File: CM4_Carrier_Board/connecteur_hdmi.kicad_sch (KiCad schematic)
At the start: 3 parts, among them J5 HDMI_A

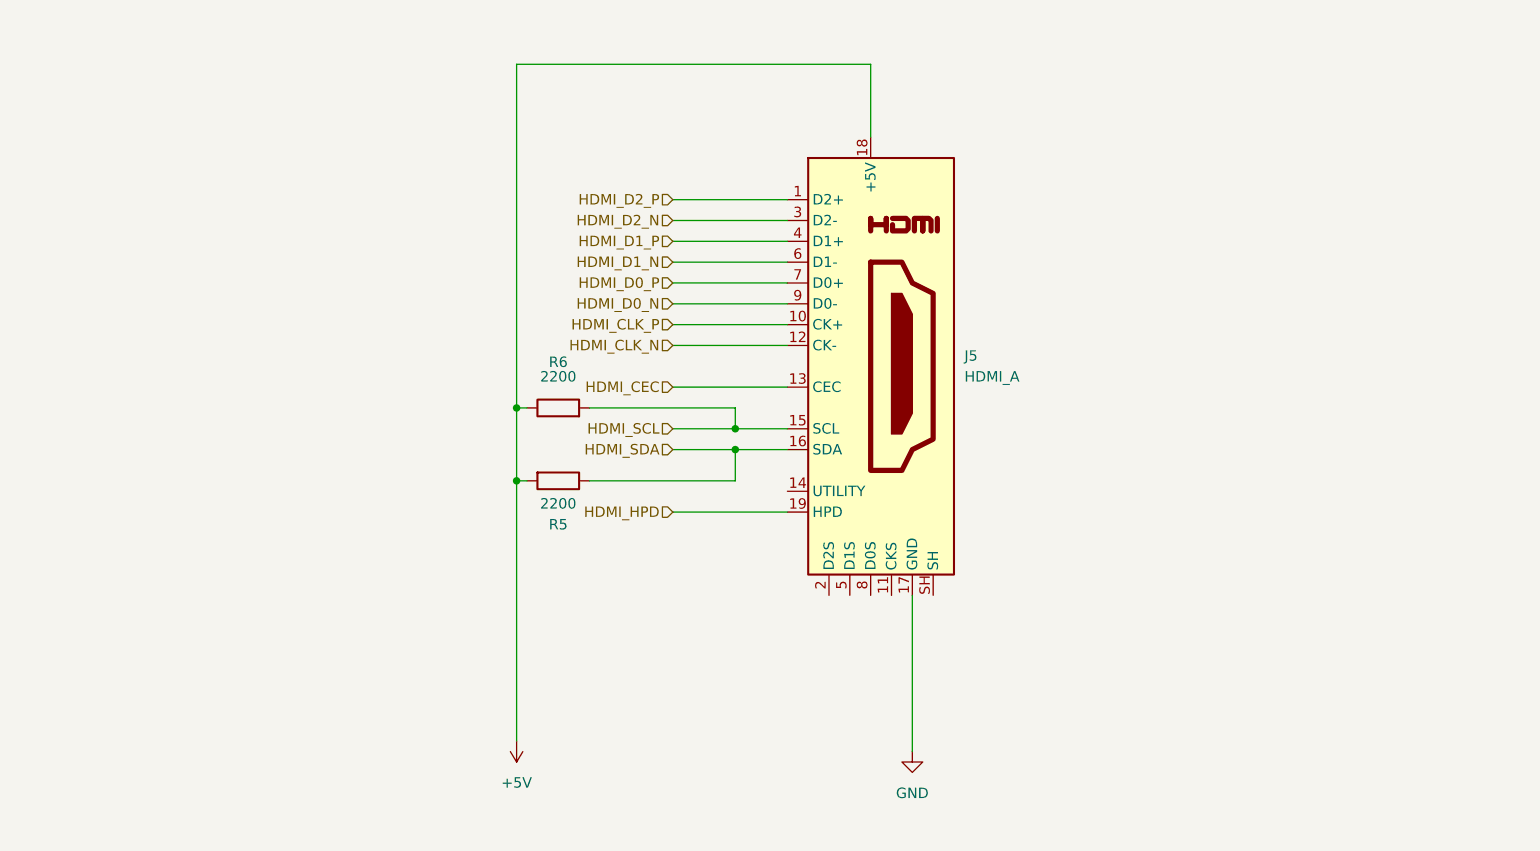
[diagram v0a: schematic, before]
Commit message: Implementation du bloc HDMI
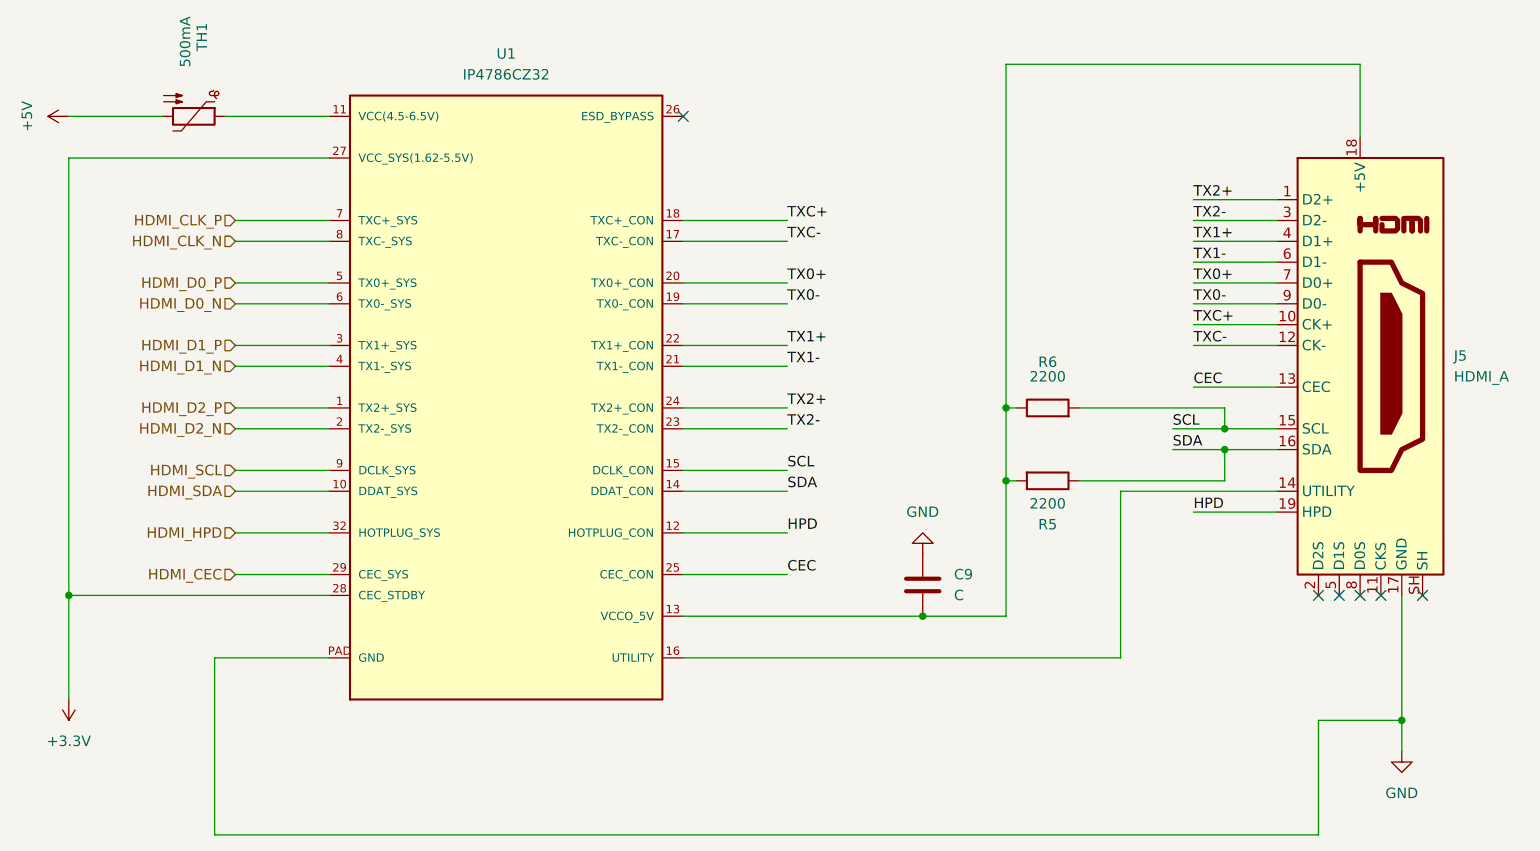
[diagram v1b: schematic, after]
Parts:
- added C9: C, symbol Device:C
- added TH1: 500mA, symbol Device:Thermistor_PTC
- added U1: IP4786CZ32, IP4786CZ32:HVQFN32, symbol IP4786CZ32:IP4786CZ32
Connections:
- net +5V: now also TH1.2; no longer J5.18 (+5V), R5.2, R6.1
- net GND: now also C9.1, U1.PAD (GND)
- net HDMI_CEC: now also U1.29 (CEC_SYS); no longer J5.13 (CEC)
- net HDMI_CLK_N: now also U1.8 (TXC-_SYS); no longer J5.12 (CK-)
- net HDMI_CLK_P: now also U1.7 (TXC+_SYS); no longer J5.10 (CK+)
- net HDMI_D0_N: now also U1.6 (TX0-_SYS); no longer J5.9 (D0-)
- net HDMI_D0_P: now also U1.5 (TX0+_SYS); no longer J5.7 (D0+)
- net HDMI_D1_N: now also U1.4 (TX1-_SYS); no longer J5.6 (D1-)
- net HDMI_D1_P: now also U1.3 (TX1+_SYS); no longer J5.4 (D1+)
- net HDMI_D2_N: now also U1.2 (TX2-_SYS); no longer J5.3 (D2-)
- net HDMI_D2_P: now also U1.1 (TX2+_SYS); no longer J5.1 (D2+)
- net HDMI_HPD: now also U1.32 (HOTPLUG_SYS); no longer J5.19 (HPD)
- net HDMI_SCL: now also U1.9 (DCLK_SYS); no longer J5.15 (SCL), R6.2
- net HDMI_SDA: now also U1.10 (DDAT_SYS); no longer J5.16 (SDA), R5.1
- net at J5.14 (UTILITY): now also U1.16 (UTILITY)
- new net: TH1.1, U1.11 (VCC(4.5-6.5V))
- new net: C9.2, J5.18 (+5V), R5.2, R6.1, U1.13 (VCCO_5V)
- new net +3.3V: U1.27 (VCC_SYS(1.62-5.5V)), U1.28 (CEC_STDBY)
- new net CEC: J5.13 (CEC), U1.25 (CEC_CON)
- new net HPD: J5.19 (HPD), U1.12 (HOTPLUG_CON)
- new net SCL: J5.15 (SCL), R6.2, U1.15 (DCLK_CON)
- new net SDA: J5.16 (SDA), R5.1, U1.14 (DDAT_CON)
- new net TX0+: J5.7 (D0+), U1.20 (TX0+_CON)
- new net TX0-: J5.9 (D0-), U1.19 (TX0-_CON)
- new net TX1+: J5.4 (D1+), U1.22 (TX1+_CON)
- new net TX1-: J5.6 (D1-), U1.21 (TX1-_CON)
- new net TX2+: J5.1 (D2+), U1.24 (TX2+_CON)
- new net TX2-: J5.3 (D2-), U1.23 (TX2-_CON)
- new net TXC+: J5.10 (CK+), U1.18 (TXC+_CON)
- new net TXC-: J5.12 (CK-), U1.17 (TXC-_CON)
- no-connect marks 0 -> 6
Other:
- moved on the sheet: J5, R5, R6

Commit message: Implémentation bloc GPIO
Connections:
- net TX0+ renamed TX0_P
- net TX0- renamed TX0_N
- net TX1+ renamed TX1_P
- net TX1- renamed TX1_N
- net TX2+ renamed TX2_P
- net TX2- renamed TX2_N
- net TXC+ renamed TXC_P
- net TXC- renamed TXC_N
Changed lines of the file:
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@@
 		)
 	)
-	(label "TXC-"
+	(label "TXC_N"
 		(at 110.49 71.12 0)
 		(effects
@@
 		)
 	)
-	(label "TX0-"
+	(label "TX0_N"
 		(at 110.49 78.74 0)
 		(effects
@@
 		)
 	)
-	(label "TXC+"
+	(label "TXC_P"
 		(at 160.02 81.28 0)
 		(effects
@@
 		)
 	)
-	(label "TX2-"
+	(label "TX2_N"
 		(at 110.49 93.98 0)
 		(effects
@@
 		)
 	)
-	(label "TX2-"
+	(label "TX2_N"
 		(at 160.02 68.58 0)
 		(effects
@@
 		)
 	)
-	(label "TXC-"
+	(label "TXC_N"
 		(at 160.02 83.82 0)
 		(effects
@@
 		)
 	)
-	(label "TX0-"
+	(label "TX0_N"
 		(at 160.02 78.74 0)
 		(effects
@@
 		)
 	)
-	(label "TX1-"
+	(label "TX1_N"
 		(at 110.49 86.36 0)
 		(effects
@@
 		)
 	)
-	(label "TX0+"
+	(label "TX0_P"
 		(at 110.49 76.2 0)
 		(effects
@@
 		)
 	)
-	(label "TX2+"
+	(label "TX2_P"
 		(at 160.02 66.04 0)
 		(effects
@@
 		)
 	)
-	(label "TX1+"
+	(label "TX1_P"
 		(at 110.49 83.82 0)
 		(effects
@@
 		)
 	)
-	(label "TXC+"
+	(label "TXC_P"
 		(at 110.49 68.58 0)
 		(effects
@@
 		)
 	)
-	(label "TX2+"
+	(label "TX2_P"
 		(at 110.49 91.44 0)
 		(effects
@@
 		)
 	)
-	(label "TX0+"
+	(label "TX0_P"
 		(at 160.02 76.2 0)
 		(effects
@@
 		)
 	)
-	(label "TX1-"
+	(label "TX1_N"
 		(at 160.02 73.66 0)
 		(effects
@@
 		)
 	)
-	(label "TX1+"
+	(label "TX1_P"
 		(at 160.02 71.12 0)
 		(effects

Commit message: Assignement des empreintes et début du PCB
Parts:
- C9: value C -> 1uF; footprint (none) -> Capacitor_SMD:C_0603_1608Metric
- J5: footprint (none) -> Connector_Video:HDMI_A_Amphenol_10029449-x01xLF_Horizontal
- R5, R6: footprint (none) -> Resistor_SMD:R_0603_1608Metric
- TH1: footprint (none) -> Fuse:Fuse_1206_3216Metric
- U1: footprint IP4786CZ32:HVQFN32 -> CM4_Carrier_Board:QFN-32-1EP_5x5mm_P0.5mm_EP3.45x3.45mm
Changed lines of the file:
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@@
+	)
+	(junction
+		(at 180.34 53.34)
+		(diameter 0)
+		(color 0 0 0 0)
 	)
 	(junction
@@
 	(wire
 		(pts
+			(xy 180.34 53.34) (xy 180.34 58.42)
+		)
+		(stroke
+			(width 0)
+			(type default)
+		)
+	)
+	(wire
+		(pts
 			(xy 175.26 129.54) (xy 185.42 129.54)
 		)
@@
 	(wire
 		(pts
-			(xy 180.34 49.53) (xy 180.34 58.42)
+			(xy 180.34 49.53) (xy 180.34 53.34)
 		)
 		(stroke
@@
 			)
 		)
-		(property "Footprint" ""
+		(property "Footprint" "Fuse:Fuse_1206_3216Metric"
 			(at 33.02 57.15 0)
 			(hide yes)
@@
 			)
 		)
-		(property "Footprint" ""
+		(property "Footprint" "Connector_Video:HDMI_A_Amphenol_10029449-x01xLF_Horizontal"
 			(at 180.975 86.36 0)
 			(hide yes)
@@
 				(path "/f7b1e63c-7624-492a-bdf8-5574ba799d92/dd2bba14-d5c1-4103-9955-c73d810f4737/f08b4a2c-4450-4c7e-9423-84109ea9e46c"
 					(reference "J5")
+					(unit 1)
+				)
+			)
+		)
+	)
+	(symbol
+		(lib_id "power:PWR_FLAG")
+		(at 180.34 53.34 270)
+		(unit 1)
+		(body_style 1)
+		(exclude_from_sim no)
+		(in_bom yes)
+		(on_board yes)
+		(in_pos_files yes)
+		(dnp no)
+		(fields_autoplaced yes)
+		(property "Reference" "#FLG05"
+			(at 182.245 53.34 0)
+			(hide yes)
+			(show_name no)
+			(do_not_autoplace no)
+			(effects
+				(font
+					(size 1.27 1.27)
+				)
+			)
+		)
+		(property "Value" "PWR_FLAG"
+			(at 184.15 53.3399 90)
+			(show_name no)
+			(do_not_autoplace no)
+			(effects
+				(font
+					(size 1.27 1.27)
+				)
+				(justify left)
+			)
+		)
+		(property "Footprint" ""
+			(at 180.34 53.34 0)
+			(hide yes)
+			(show_name no)
+			(do_not_autoplace no)
+			(effects
+				(font
+					(size 1.27 1.27)
+				)
+			)
+		)
+		(property "Datasheet" ""
+			(at 180.34 53.34 0)
+			(hide yes)
+			(show_name no)
+			(do_not_autoplace no)
+			(effects
+				(font
+					(size 1.27 1.27)
+				)
+			)
+		)
+		(property "Description" "Special symbol for telling ERC where power comes from"
+			(at 180.34 53.34 0)
+			(hide yes)
+			(show_name no)
+			(do_not_autoplace no)
+			(effects
+				(font
+					(size 1.27 1.27)
+				)
+			)
+		)
+		(pin "1"
+		)
+		(instances
+			(project "CM4_Carrier_Board"
+				(path "/f7b1e63c-7624-492a-bdf8-5574ba799d92/dd2bba14-d5c1-4103-9955-c73d810f4737/f08b4a2c-4450-4c7e-9423-84109ea9e46c"
+					(reference "#FLG05")
 					(unit 1)
 				)
@@
 			)
 		)
-		(property "Value" "C"
+		(property "Value" "1uF"
 			(at 130.81 114.2999 0)
 			(show_name no)
@@
 			)
 		)
-		(property "Footprint" ""
+		(property "Footprint" "Capacitor_SMD:C_0603_1608Metric"
 			(at 127.9652 116.84 0)
 			(hide yes)
@@
 			)
 		)
-		(property "Footprint" ""
+		(property "Footprint" "Resistor_SMD:R_0603_1608Metric"
 			(at 142.24 93.218 90)
 			(hide yes)
@@
 			)
 		)
-		(property "Footprint" ""
+		(property "Footprint" "Resistor_SMD:R_0603_1608Metric"
 			(at 142.24 98.552 90)
 			(hide yes)
@@
 			)
 		)
-		(property "Footprint" "IP4786CZ32:HVQFN32"
+		(property "Footprint" "CM4_Carrier_Board:QFN-32-1EP_5x5mm_P0.5mm_EP3.45x3.45mm"
 			(at 77.47 88.9 0)
 			(hide yes)
